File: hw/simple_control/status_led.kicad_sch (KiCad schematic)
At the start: 4 parts, among them Q2 BC817

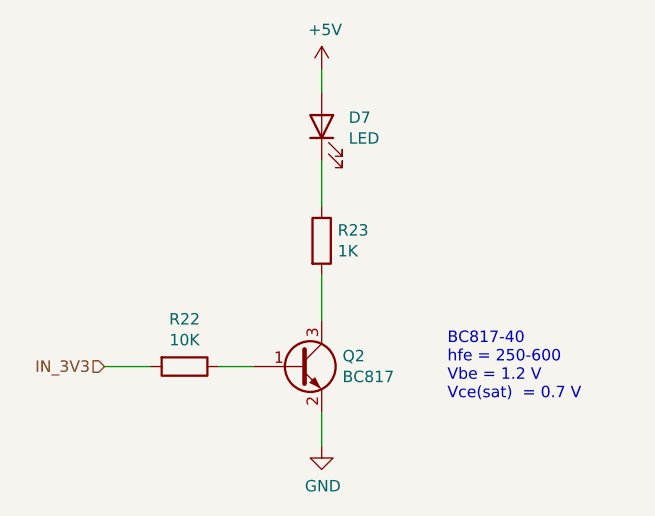
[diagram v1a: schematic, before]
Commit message: [hw] Wire some RPi Pico/Zero connections
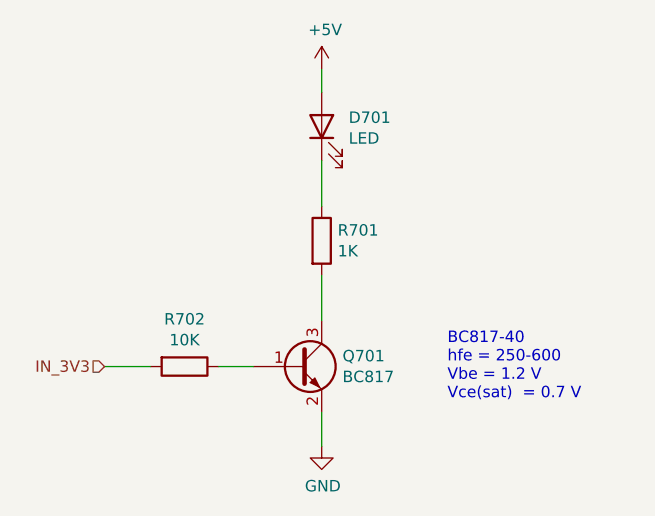
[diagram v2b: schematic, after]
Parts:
- renumbered D7 to D701, Q2 to Q701, R23 to R701, R22 to R702
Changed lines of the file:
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@@
   (symbol (lib_id "Device:Q_NPN_BEC") (at 127 109.22 0) (unit 1)
     (in_bom yes) (on_board yes) (dnp no)
-    (property "Reference" "Q2" (at 131.8514 108.0516 0)
+    (property "Reference" "Q701" (at 131.8514 108.0516 0)
       (effects (font (size 1.27 1.27)) (justify left))
     )
@@
       (project "simple_control"
         (path "/063164e8-0d2a-492b-8a61-e4fa4fbf06a6/3d4e7106-28aa-4335-9fa1-cc7761972854/90456e74-ff8a-472d-a77b-f456718516e1"
-          (reference "Q2") (unit 1)
-        )
-        (path "/063164e8-0d2a-492b-8a61-e4fa4fbf06a6/3d4e7106-28aa-4335-9fa1-cc7761972854/6dfa3ccc-9562-40f4-be33-9e56e01c25ee"
-          (reference "Q3") (unit 1)
-        )
-        (path "/063164e8-0d2a-492b-8a61-e4fa4fbf06a6/3d4e7106-28aa-4335-9fa1-cc7761972854/b2425a51-288c-487b-a5cd-94ea45276123"
-          (reference "Q4") (unit 1)
-        )
-        (path "/063164e8-0d2a-492b-8a61-e4fa4fbf06a6/3d4e7106-28aa-4335-9fa1-cc7761972854/73523822-726f-497f-999a-d02a38eec383"
-          (reference "Q5") (unit 1)
+          (reference "Q701") (unit 1)
+        )
+        (path "/063164e8-0d2a-492b-8a61-e4fa4fbf06a6/3d4e7106-28aa-4335-9fa1-cc7761972854/6dfa3ccc-9562-40f4-be33-9e56e01c25ee"
+          (reference "Q801") (unit 1)
+        )
+        (path "/063164e8-0d2a-492b-8a61-e4fa4fbf06a6/3d4e7106-28aa-4335-9fa1-cc7761972854/b2425a51-288c-487b-a5cd-94ea45276123"
+          (reference "Q901") (unit 1)
+        )
+        (path "/063164e8-0d2a-492b-8a61-e4fa4fbf06a6/3d4e7106-28aa-4335-9fa1-cc7761972854/73523822-726f-497f-999a-d02a38eec383"
+          (reference "Q1001") (unit 1)
         )
       )
@@
   (symbol (lib_id "Device:R") (at 129.54 95.25 0) (unit 1)
     (in_bom yes) (on_board yes) (dnp no)
-    (property "Reference" "R23" (at 131.318 94.0816 0)
+    (property "Reference" "R701" (at 131.318 94.0816 0)
       (effects (font (size 1.27 1.27)) (justify left))
     )
@@
       (project "simple_control"
         (path "/063164e8-0d2a-492b-8a61-e4fa4fbf06a6/3d4e7106-28aa-4335-9fa1-cc7761972854/90456e74-ff8a-472d-a77b-f456718516e1"
-          (reference "R23") (unit 1)
-        )
-        (path "/063164e8-0d2a-492b-8a61-e4fa4fbf06a6/3d4e7106-28aa-4335-9fa1-cc7761972854/6dfa3ccc-9562-40f4-be33-9e56e01c25ee"
-          (reference "R25") (unit 1)
-        )
-        (path "/063164e8-0d2a-492b-8a61-e4fa4fbf06a6/3d4e7106-28aa-4335-9fa1-cc7761972854/b2425a51-288c-487b-a5cd-94ea45276123"
-          (reference "R27") (unit 1)
-        )
-        (path "/063164e8-0d2a-492b-8a61-e4fa4fbf06a6/3d4e7106-28aa-4335-9fa1-cc7761972854/73523822-726f-497f-999a-d02a38eec383"
-          (reference "R29") (unit 1)
+          (reference "R701") (unit 1)
+        )
+        (path "/063164e8-0d2a-492b-8a61-e4fa4fbf06a6/3d4e7106-28aa-4335-9fa1-cc7761972854/6dfa3ccc-9562-40f4-be33-9e56e01c25ee"
+          (reference "R801") (unit 1)
+        )
+        (path "/063164e8-0d2a-492b-8a61-e4fa4fbf06a6/3d4e7106-28aa-4335-9fa1-cc7761972854/b2425a51-288c-487b-a5cd-94ea45276123"
+          (reference "R901") (unit 1)
+        )
+        (path "/063164e8-0d2a-492b-8a61-e4fa4fbf06a6/3d4e7106-28aa-4335-9fa1-cc7761972854/73523822-726f-497f-999a-d02a38eec383"
+          (reference "R1001") (unit 1)
         )
       )
@@
   (symbol (lib_id "Device:R") (at 114.3 109.22 270) (unit 1)
     (in_bom yes) (on_board yes) (dnp no)
-    (property "Reference" "R22" (at 114.3 103.9622 90)
+    (property "Reference" "R702" (at 114.3 103.9622 90)
       (effects (font (size 1.27 1.27)))
     )
@@
       (project "simple_control"
         (path "/063164e8-0d2a-492b-8a61-e4fa4fbf06a6/3d4e7106-28aa-4335-9fa1-cc7761972854/90456e74-ff8a-472d-a77b-f456718516e1"
-          (reference "R22") (unit 1)
-        )
-        (path "/063164e8-0d2a-492b-8a61-e4fa4fbf06a6/3d4e7106-28aa-4335-9fa1-cc7761972854/6dfa3ccc-9562-40f4-be33-9e56e01c25ee"
-          (reference "R24") (unit 1)
-        )
-        (path "/063164e8-0d2a-492b-8a61-e4fa4fbf06a6/3d4e7106-28aa-4335-9fa1-cc7761972854/b2425a51-288c-487b-a5cd-94ea45276123"
-          (reference "R26") (unit 1)
-        )
-        (path "/063164e8-0d2a-492b-8a61-e4fa4fbf06a6/3d4e7106-28aa-4335-9fa1-cc7761972854/73523822-726f-497f-999a-d02a38eec383"
-          (reference "R28") (unit 1)
+          (reference "R702") (unit 1)
+        )
+        (path "/063164e8-0d2a-492b-8a61-e4fa4fbf06a6/3d4e7106-28aa-4335-9fa1-cc7761972854/6dfa3ccc-9562-40f4-be33-9e56e01c25ee"
+          (reference "R802") (unit 1)
+        )
+        (path "/063164e8-0d2a-492b-8a61-e4fa4fbf06a6/3d4e7106-28aa-4335-9fa1-cc7761972854/b2425a51-288c-487b-a5cd-94ea45276123"
+          (reference "R902") (unit 1)
+        )
+        (path "/063164e8-0d2a-492b-8a61-e4fa4fbf06a6/3d4e7106-28aa-4335-9fa1-cc7761972854/73523822-726f-497f-999a-d02a38eec383"
+          (reference "R1002") (unit 1)
         )
       )
@@
   (symbol (lib_id "power:+5V") (at 129.54 76.2 0) (unit 1)
     (in_bom yes) (on_board yes) (dnp no)
-    (property "Reference" "#PWR021" (at 129.54 80.01 0)
+    (property "Reference" "#PWR0701" (at 129.54 80.01 0)
       (effects (font (size 1.27 1.27)) hide)
     )
@@
       (project "simple_control"
         (path "/063164e8-0d2a-492b-8a61-e4fa4fbf06a6/3d4e7106-28aa-4335-9fa1-cc7761972854/90456e74-ff8a-472d-a77b-f456718516e1"
-          (reference "#PWR021") (unit 1)
-        )
-        (path "/063164e8-0d2a-492b-8a61-e4fa4fbf06a6/3d4e7106-28aa-4335-9fa1-cc7761972854/6dfa3ccc-9562-40f4-be33-9e56e01c25ee"
-          (reference "#PWR023") (unit 1)
-        )
-        (path "/063164e8-0d2a-492b-8a61-e4fa4fbf06a6/3d4e7106-28aa-4335-9fa1-cc7761972854/b2425a51-288c-487b-a5cd-94ea45276123"
-          (reference "#PWR025") (unit 1)
-        )
-        (path "/063164e8-0d2a-492b-8a61-e4fa4fbf06a6/3d4e7106-28aa-4335-9fa1-cc7761972854/73523822-726f-497f-999a-d02a38eec383"
-          (reference "#PWR027") (unit 1)
+          (reference "#PWR0701") (unit 1)
+        )
+        (path "/063164e8-0d2a-492b-8a61-e4fa4fbf06a6/3d4e7106-28aa-4335-9fa1-cc7761972854/6dfa3ccc-9562-40f4-be33-9e56e01c25ee"
+          (reference "#PWR0801") (unit 1)
+        )
+        (path "/063164e8-0d2a-492b-8a61-e4fa4fbf06a6/3d4e7106-28aa-4335-9fa1-cc7761972854/b2425a51-288c-487b-a5cd-94ea45276123"
+          (reference "#PWR0901") (unit 1)
+        )
+        (path "/063164e8-0d2a-492b-8a61-e4fa4fbf06a6/3d4e7106-28aa-4335-9fa1-cc7761972854/73523822-726f-497f-999a-d02a38eec383"
+          (reference "#PWR01001") (unit 1)
         )
       )
@@
   (symbol (lib_id "power:GND") (at 129.54 118.11 0) (unit 1)
     (in_bom yes) (on_board yes) (dnp no)
-    (property "Reference" "#PWR022" (at 129.54 124.46 0)
+    (property "Reference" "#PWR0702" (at 129.54 124.46 0)
       (effects (font (size 1.27 1.27)) hide)
     )
@@
       (project "simple_control"
         (path "/063164e8-0d2a-492b-8a61-e4fa4fbf06a6/3d4e7106-28aa-4335-9fa1-cc7761972854/90456e74-ff8a-472d-a77b-f456718516e1"
-          (reference "#PWR022") (unit 1)
-        )
-        (path "/063164e8-0d2a-492b-8a61-e4fa4fbf06a6/3d4e7106-28aa-4335-9fa1-cc7761972854/6dfa3ccc-9562-40f4-be33-9e56e01c25ee"
-          (reference "#PWR024") (unit 1)
-        )
-        (path "/063164e8-0d2a-492b-8a61-e4fa4fbf06a6/3d4e7106-28aa-4335-9fa1-cc7761972854/b2425a51-288c-487b-a5cd-94ea45276123"
-          (reference "#PWR026") (unit 1)
-        )
-        (path "/063164e8-0d2a-492b-8a61-e4fa4fbf06a6/3d4e7106-28aa-4335-9fa1-cc7761972854/73523822-726f-497f-999a-d02a38eec383"
-          (reference "#PWR028") (unit 1)
+          (reference "#PWR0702") (unit 1)
+        )
+        (path "/063164e8-0d2a-492b-8a61-e4fa4fbf06a6/3d4e7106-28aa-4335-9fa1-cc7761972854/6dfa3ccc-9562-40f4-be33-9e56e01c25ee"
+          (reference "#PWR0802") (unit 1)
+        )
+        (path "/063164e8-0d2a-492b-8a61-e4fa4fbf06a6/3d4e7106-28aa-4335-9fa1-cc7761972854/b2425a51-288c-487b-a5cd-94ea45276123"
+          (reference "#PWR0902") (unit 1)
+        )
+        (path "/063164e8-0d2a-492b-8a61-e4fa4fbf06a6/3d4e7106-28aa-4335-9fa1-cc7761972854/73523822-726f-497f-999a-d02a38eec383"
+          (reference "#PWR01002") (unit 1)
         )
       )
@@
   (symbol (lib_id "Device:LED") (at 129.54 82.55 90) (unit 1)
     (in_bom yes) (on_board yes) (dnp no)
-    (property "Reference" "D7" (at 132.5372 81.5594 90)
+    (property "Reference" "D701" (at 132.5372 81.5594 90)
       (effects (font (size 1.27 1.27)) (justify right))
     )
@@
       (project "simple_control"
         (path "/063164e8-0d2a-492b-8a61-e4fa4fbf06a6/3d4e7106-28aa-4335-9fa1-cc7761972854/90456e74-ff8a-472d-a77b-f456718516e1"
-          (reference "D7") (unit 1)
-        )
-        (path "/063164e8-0d2a-492b-8a61-e4fa4fbf06a6/3d4e7106-28aa-4335-9fa1-cc7761972854/6dfa3ccc-9562-40f4-be33-9e56e01c25ee"
-          (reference "D8") (unit 1)
-        )
-        (path "/063164e8-0d2a-492b-8a61-e4fa4fbf06a6/3d4e7106-28aa-4335-9fa1-cc7761972854/b2425a51-288c-487b-a5cd-94ea45276123"
-          (reference "D9") (unit 1)
-        )
-        (path "/063164e8-0d2a-492b-8a61-e4fa4fbf06a6/3d4e7106-28aa-4335-9fa1-cc7761972854/73523822-726f-497f-999a-d02a38eec383"
-          (reference "D10") (unit 1)
-        )
-      )
+          (reference "D701") (unit 1)
+        )
+        (path "/063164e8-0d2a-492b-8a61-e4fa4fbf06a6/3d4e7106-28aa-4335-9fa1-cc7761972854/6dfa3ccc-9562-40f4-be33-9e56e01c25ee"
+          (reference "D801") (unit 1)
+        )
+        (path "/063164e8-0d2a-492b-8a61-e4fa4fbf06a6/3d4e7106-28aa-4335-9fa1-cc7761972854/b2425a51-288c-487b-a5cd-94ea45276123"
+          (reference "D901") (unit 1)
+        )
+        (path "/063164e8-0d2a-492b-8a61-e4fa4fbf06a6/3d4e7106-28aa-4335-9fa1-cc7761972854/73523822-726f-497f-999a-d02a38eec383"
+          (reference "D1001") (unit 1)
+        )
+      )
